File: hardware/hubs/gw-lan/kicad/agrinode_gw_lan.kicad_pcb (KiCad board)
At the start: 2 copper layers, 150 x 108 mm, 126 parts, among them J1 DC 12V 5.5/2.1, J10 LAN, J2 DC IN 7-24V, J3 SOLAR 6-24V, J4 USB 5V / PROG, J5 BAT NTC 10k, J6 PROG, J7 I2C, J8 LED STRIP WS2813, J9 RS-485, Q1 AO3401A, Q2 AO3401A, Q3 MMBT3904, Q4 MMBT3904, Q5 BSS138, Q6 MMBT3904, SW1 RESET, SW2 BOOT / PAIR, U1 LM2596S-5.0, U2 TP4056, U3 MIC29302WU, U4 ESP32-WROOM-32E-N8, U5 CH340C, U6 DS3231MZ, U7 MAX3485ESA, U8 Ra-02 SX1278 433MHz, U9 ENC28J60-I/SO, Y1 25MHz

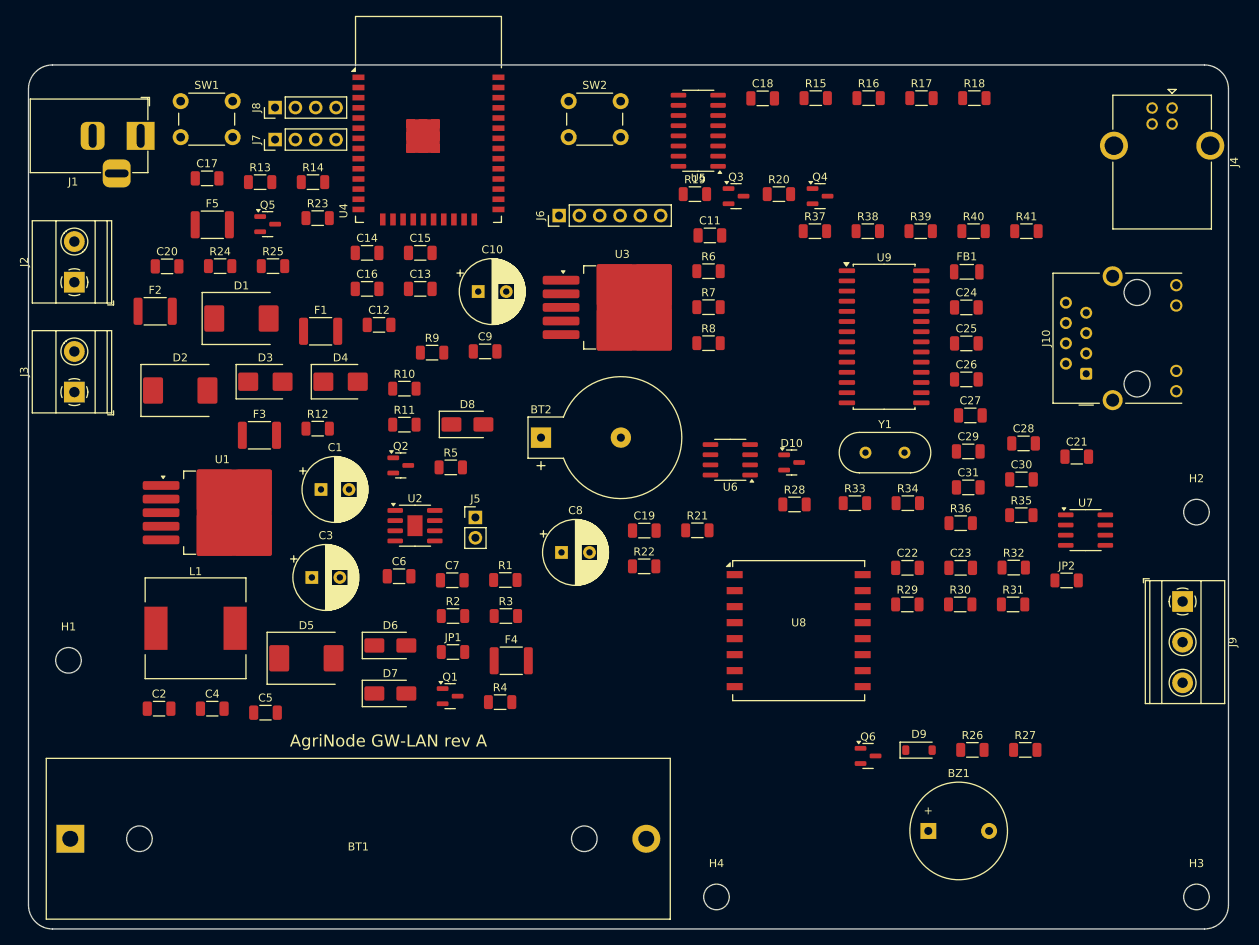
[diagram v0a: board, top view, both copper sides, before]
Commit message: GW-LAN: fully routed (0 unconnected, 0 clearance errors, no jumpers), 150x108 mm; renders, Gerbers, README status
Co-Authored-By: Claude Opus 5.5 <noreply@anthropic.com>
Claude-Session: https://claude.ai/code/session_014J7amXZ5Y6AZWEh5CjDNja
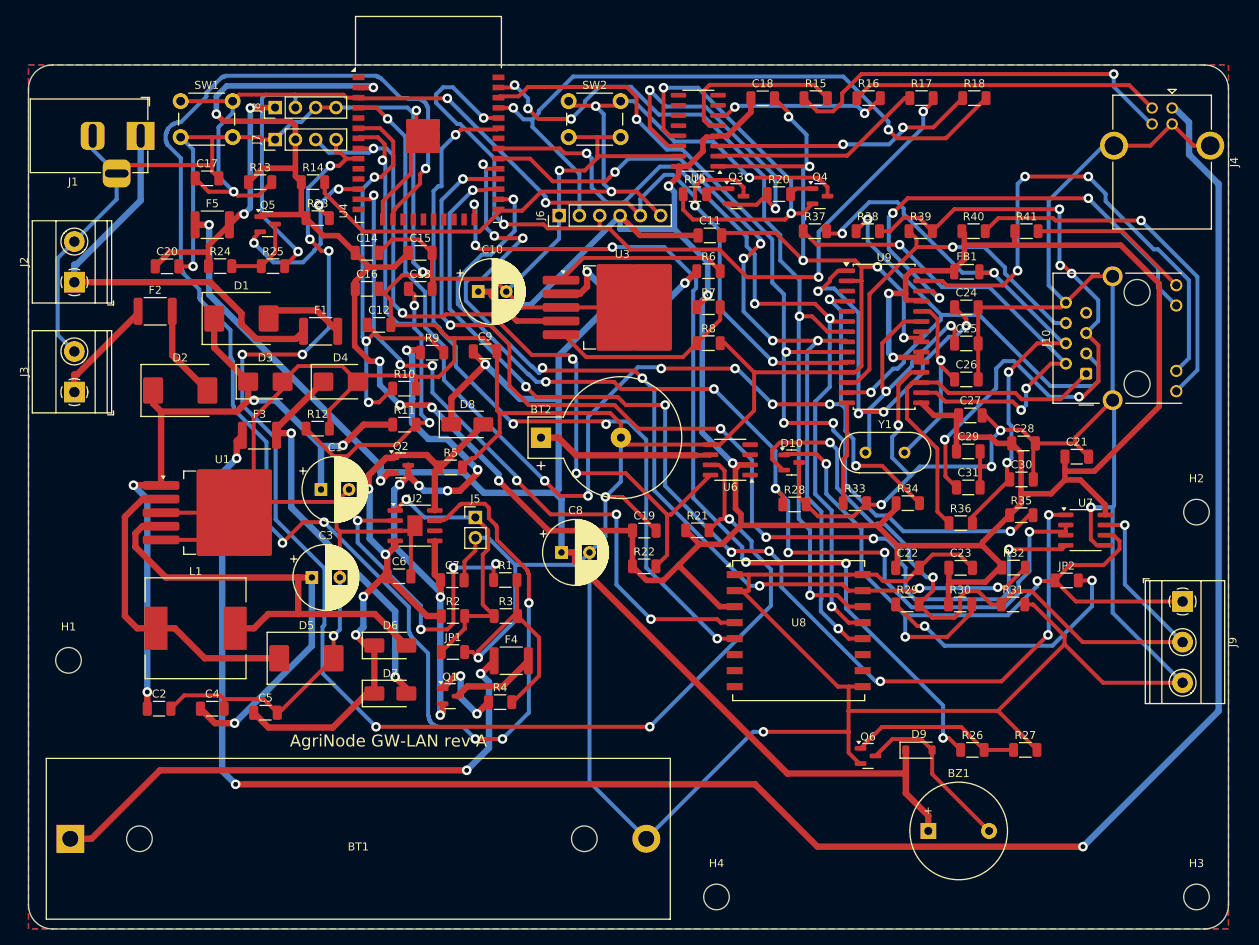
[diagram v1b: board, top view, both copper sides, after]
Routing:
- net GND: track 0.00 -> 1088.6 mm, vias 0 -> 18
- net +3V3: track 0.00 -> 482.1 mm, vias 0 -> 11
- net /Power - 12V, solar and USB inputs, 18650 charger, rails/VUSB_RAW: track 0.00 -> 256.5 mm, vias 0 -> 3
- net VSYS: track 0.00 -> 213.5 mm, vias 0 -> 5
- net CHRG_N: track 0.00 -> 196.2 mm, vias 0 -> 6
- net /ESP32, programming, buttons, RTC, LED strip, buzzer/I2C_SDA: track 0.00 -> 175.9 mm, vias 0 -> 8
- net ETH_INT: track 0.00 -> 144.1 mm, vias 0 -> 9
- net ESP_EN: track 0.00 -> 144.0 mm, vias 0 -> 5
- net RS485_RX: track 0.00 -> 140.9 mm, vias 0 -> 8
- net RS485_TX: track 0.00 -> 131.3 mm, vias 0 -> 6
- net RS485_DE: track 0.00 -> 130.2 mm, vias 0 -> 7
- net LORA_CS: track 0.00 -> 121.6 mm, vias 0 -> 8
- net /ESP32, programming, buttons, RTC, LED strip, buzzer/BUZZER_CTL: track 0.00 -> 117.2 mm, vias 0 -> 6
- net ETH_CS: track 0.00 -> 117.0 mm, vias 0 -> 5
- net SPI_MOSI: track 0.00 -> 111.1 mm, vias 0 -> 5
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- added copper zone on B.Cu, net GND
- added copper zone on F.Cu, net GND
